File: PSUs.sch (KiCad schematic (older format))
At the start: 26 parts, among them U1 LM2674N-ADJ, U11 MCP4151-103E/P, U12 MCP4151-103E/P, U3 LM2674N-ADJ, U8 MCP6042

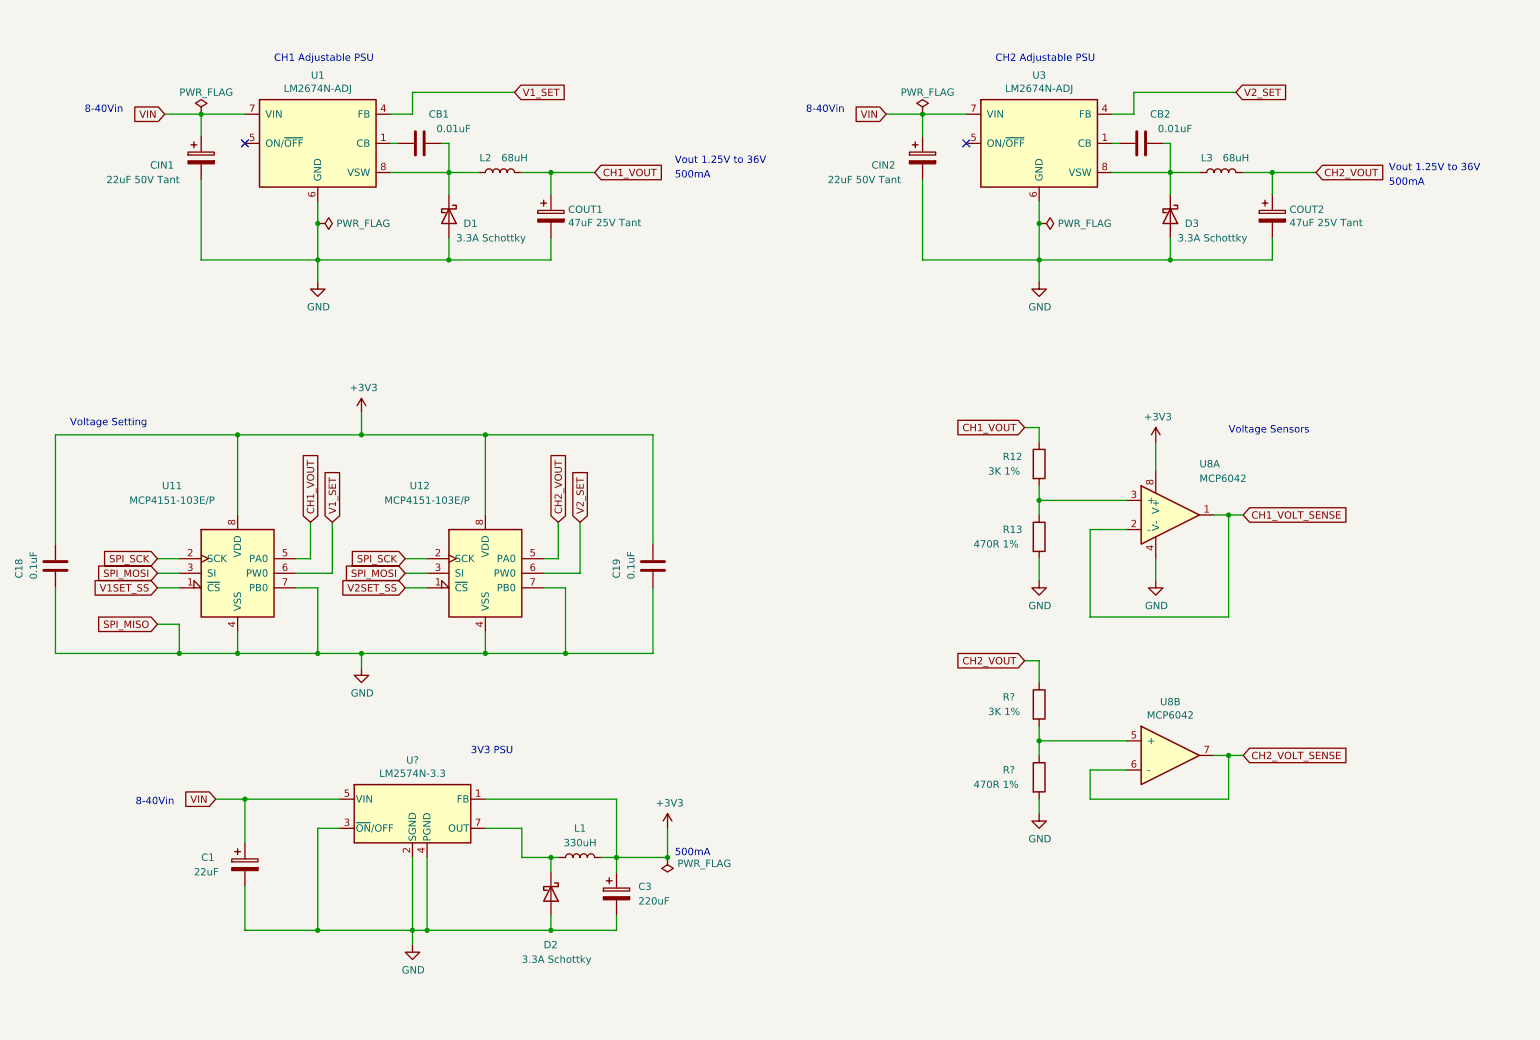
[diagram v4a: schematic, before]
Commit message: fixed some DRC errors
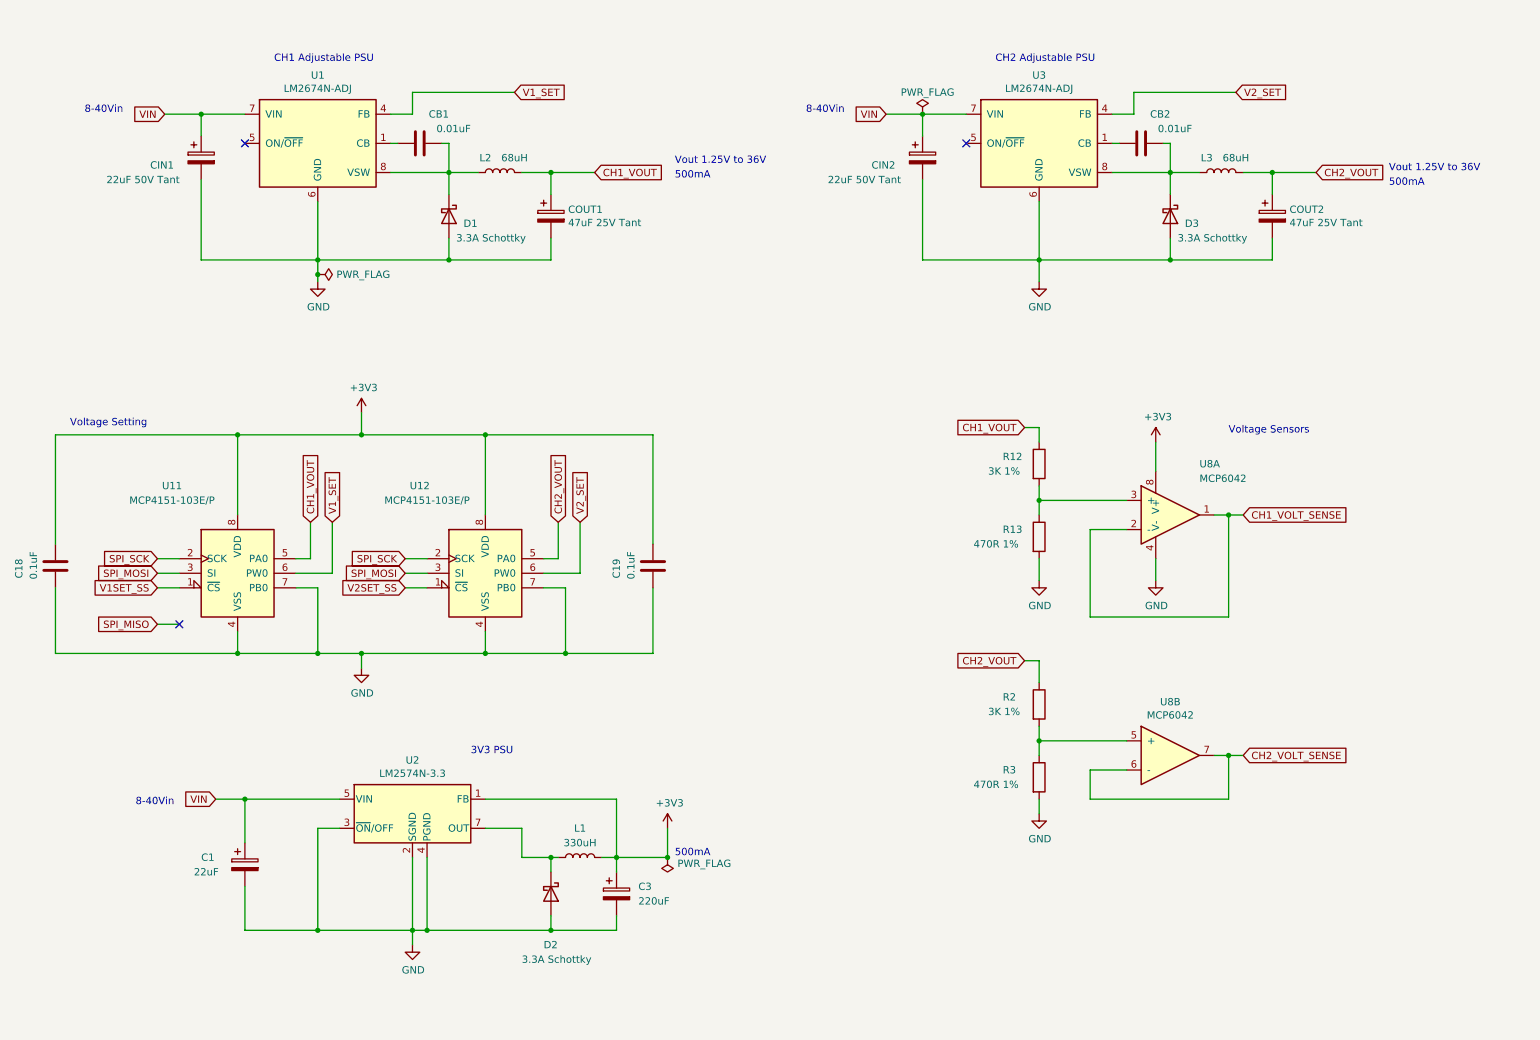
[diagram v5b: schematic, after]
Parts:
- gave numbers to parts that had none: 3
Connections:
- no-connect marks 2 -> 3
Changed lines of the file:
@@
 Wire Wire Line
 	8700 2400 7800 2400
-Wire Wire Line
-	7800 2400 7800 2150
 Connection ~ 8700 2400
 NoConn ~ 7300 1600
@@
 Text Notes 6200 1400 0    50   ~ 0
 8-40Vin
-$Comp
-L power:PWR_FLAG #GNDFLAG?
-U 1 1 605245E4
-P 7800 2150
-AR Path="/605245E4" Ref="#GNDFLAG?"  Part="1"
-AR Path="/604D3BA3/605245E4" Ref="#GNDFLAG0101"  Part="1"
-F 0 "#GNDFLAG0101" H 7800 2225 50  0001 C CNN
-F 1 "PWR_FLAG" V 7800 2278 50  0000 L CNN
-F 2 "" H 7800 2150 50  0001 C CNN
-F 3 "~" H 7800 2150 50  0001 C CNN
-	1    7800 2150
-	0    1    1    0
-$EndComp
-Connection ~ 7800 2150
-Wire Wire Line
-	7800 2150 7800 2000
 Text Notes 7500 1050 0    50   ~ 0
 CH2 Adjustable PSU
 Text Notes 2550 1050 0    50   ~ 0
 CH1 Adjustable PSU
-Wire Wire Line
-	2850 2150 2850 2000
-Connection ~ 2850 2150
-$Comp
-L power:PWR_FLAG #GNDFLAG?
-U 1 1 605245F3
-P 2850 2150
-AR Path="/605245F3" Ref="#GNDFLAG?"  Part="1"
-AR Path="/604D3BA3/605245F3" Ref="#GNDFLAG0102"  Part="1"
-F 0 "#GNDFLAG0102" H 2850 2225 50  0001 C CNN
-F 1 "PWR_FLAG" V 2850 2278 50  0000 L CNN
-F 2 "" H 2850 2150 50  0001 C CNN
-F 3 "~" H 2850 2150 50  0001 C CNN
-	1    2850 2150
-	0    1    1    0
-$EndComp
 Text Notes 1250 1400 0    50   ~ 0
 8-40Vin
-$Comp
-L power:PWR_FLAG #8-40Vin?
-U 1 1 605245FA
-P 2050 1400
-AR Path="/605245FA" Ref="#8-40Vin?"  Part="1"
-AR Path="/604D3BA3/605245FA" Ref="#8-40Vin0102"  Part="1"
-F 0 "#8-40Vin0102" H 2050 1475 50  0001 C CNN
-F 1 "PWR_FLAG" H 1900 1550 50  0000 L CNN
-F 2 "" H 2050 1400 50  0001 C CNN
-F 3 "~" H 2050 1400 50  0001 C CNN
-	1    2050 1400
-	1    0    0    -1
-$EndComp
 $Comp
 L Regulator_Switching:LM2674N-ADJ U?
@@
 Wire Wire Line
 	3350 1600 3400 1600
-Connection ~ 2050 1400
-Wire Wire Line
-	2050 1400 1800 1400
 Wire Wire Line
 	2050 2400 2850 2400
 Wire Wire Line
 	2050 1850 2050 2400
-Wire Wire Line
-	2050 1400 2050 1550
-Wire Wire Line
-	2350 1400 2050 1400
 Wire Wire Line
 	4450 1800 4750 1800
@@
 $EndComp
 Wire Wire Line
-	2850 2400 2850 2550
+	2850 2400 2850 2500
 Text GLabel 1800 1400 0    50   Input ~ 0
 VIN
@@
 NoConn ~ 2350 1600
 Connection ~ 3750 2400
-Wire Wire Line
-	2850 2400 2850 2150
 Wire Wire Line
 	3750 2400 2850 2400
@@
 Wire Wire Line
 	1050 4650 1050 5100
-Wire Wire Line
-	1050 5100 1900 5100
 Connection ~ 2300 5100
 $Comp
@@
 Wire Wire Line
 	4000 3600 3150 3600
-Text GLabel 1750 4900 0    50   Input ~ 0
-SPI_MISO
-Wire Wire Line
-	1750 4900 1900 4900
-Wire Wire Line
-	1900 4900 1900 5100
-Connection ~ 1900 5100
-Wire Wire Line
-	1900 5100 2300 5100
 Text GLabel 1750 4450 0    50   Input ~ 0
 SPI_SCK
@@
 SPI_MOSI
 $Comp
-L power:+3V3 #PWR?
+L power:+3V3 #PWR0103
 U 1 1 600D52AF
 P 5250 6300
-F 0 "#PWR?" H 5250 6150 50  0001 C CNN
+F 0 "#PWR0103" H 5250 6150 50  0001 C CNN
 F 1 "+3V3" H 5265 6473 50  0000 C CNN
 F 2 "" H 5250 6300 50  0001 C CNN
@@
 $EndComp
 $Comp
-L power:+3V3 #PWR?
+L power:+3V3 #PWR0105
 U 1 1 600D6FEA
 P 8600 3650
-F 0 "#PWR?" H 8600 3500 50  0001 C CNN
+F 0 "#PWR0105" H 8600 3500 50  0001 C CNN
 F 1 "+3V3" H 8615 3823 50  0000 C CNN
 F 2 "" H 8600 3650 50  0001 C CNN
@@
 $EndComp
 $Comp
-L power:+3V3 #PWR?
+L power:+3V3 #PWR0107
 U 1 1 600D7AC4
 P 3150 3450
-F 0 "#PWR?" H 3150 3300 50  0001 C CNN
+F 0 "#PWR0107" H 3150 3300 50  0001 C CNN
 F 1 "+3V3" H 3165 3623 50  0000 C CNN
 F 2 "" H 3150 3450 50  0001 C CNN
@@
 $EndComp
 $Comp
-L Device:R R?
+L Device:R R2
 U 1 1 600E45EF
 P 7800 5450
-F 0 "R?" H 7550 5500 50  0000 L CNN
+F 0 "R2" H 7550 5500 50  0000 L CNN
 F 1 "3K 1%" H 7450 5400 50  0000 L CNN
 F 2 "" V 7730 5450 50  0001 C CNN
@@
 $EndComp
 $Comp
-L Device:R R?
+L Device:R R3
 U 1 1 600E4D4D
 P 7800 5950
-F 0 "R?" H 7550 6000 50  0000 L CNN
+F 0 "R3" H 7550 6000 50  0000 L CNN
 F 1 "470R 1%" H 7350 5900 50  0000 L CNN
 F 2 "" V 7730 5950 50  0001 C CNN
@@
 $EndComp
 $Comp
-L Regulator_Switching:LM2574N-3.3 U?
+L Regulator_Switching:LM2574N-3.3 U2
 U 1 1 600E5721
 P 3500 6200
-F 0 "U?" H 3500 6567 50  0000 C CNN
+F 0 "U2" H 3500 6567 50  0000 C CNN
 F 1 "LM2574N-3.3" H 3500 6476 50  0000 C CNN
 F 2 "Package_DIP:DIP-8_W7.62mm" H 3100 6550 50  0001 L CIN
@@
 Wire Wire Line
 	3600 7000 4450 7000
+Wire Wire Line
+	7800 2000 7800 2400
+Wire Wire Line
+	2850 2000 2850 2400
+Wire Wire Line
+	2350 1400 2050 1400
+Wire Wire Line
+	2050 1550 2050 1400
+Connection ~ 2050 1400
+Wire Wire Line
+	2050 1400 1800 1400
+$Comp
+L power:PWR_FLAG #FLG0101
+U 1 1 5FF5E115
+P 2850 2500
+F 0 "#FLG0101" H 2850 2575 50  0001 C CNN
+F 1 "PWR_FLAG" V 2850 2628 50  0000 L CNN
+F 2 "" H 2850 2500 50  0001 C CNN
+F 3 "~" H 2850 2500 50  0001 C CNN
+	1    2850 2500
+	0    1    1    0
+$EndComp
+Connection ~ 2850 2500
+Wire Wire Line
+	2850 2500 2850 2550
+Wire Wire Line
+	1750 4900 1900 4900
+Text GLabel 1750 4900 0    50   Input ~ 0
+SPI_MISO
+Wire Wire Line
+	1050 5100 2300 5100
+NoConn ~ 1900 4900
 $EndSCHEMATC

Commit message: ported over LCD display code, modified schematic as we no longer need some of the I2C expanders
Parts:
- U1, U2, U3: footprint Package_DIP:DIP-8_W7.62mm -> (none)
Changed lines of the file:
@@
 F 0 "U3" H 7800 2067 50  0000 C CNN
 F 1 "LM2674N-ADJ" H 7800 1976 50  0000 C CNN
-F 2 "Package_DIP:DIP-8_W7.62mm" H 7850 1250 50  0001 L CIN
+F 2 "" H 7850 1250 50  0001 L CIN
 F 3 "http://www.ti.com/lit/ds/symlink/lm2674.pdf" H 7800 1600 50  0001 C CNN
 	1    7800 1600
@@
 F 0 "U1" H 2850 2067 50  0000 C CNN
 F 1 "LM2674N-ADJ" H 2850 1976 50  0000 C CNN
-F 2 "Package_DIP:DIP-8_W7.62mm" H 2900 1250 50  0001 L CIN
+F 2 "" H 2900 1250 50  0001 L CIN
 F 3 "http://www.ti.com/lit/ds/symlink/lm2674.pdf" H 2850 1600 50  0001 C CNN
 	1    2850 1600
@@
 F 0 "U2" H 3500 6567 50  0000 C CNN
 F 1 "LM2574N-3.3" H 3500 6476 50  0000 C CNN
-F 2 "Package_DIP:DIP-8_W7.62mm" H 3100 6550 50  0001 L CIN
+F 2 "" H 3100 6550 50  0001 L CIN
 F 3 "http://www.national.com/ds/LM/LM2574.pdf" H 3500 6200 50  0001 C CNN
 	1    3500 6200

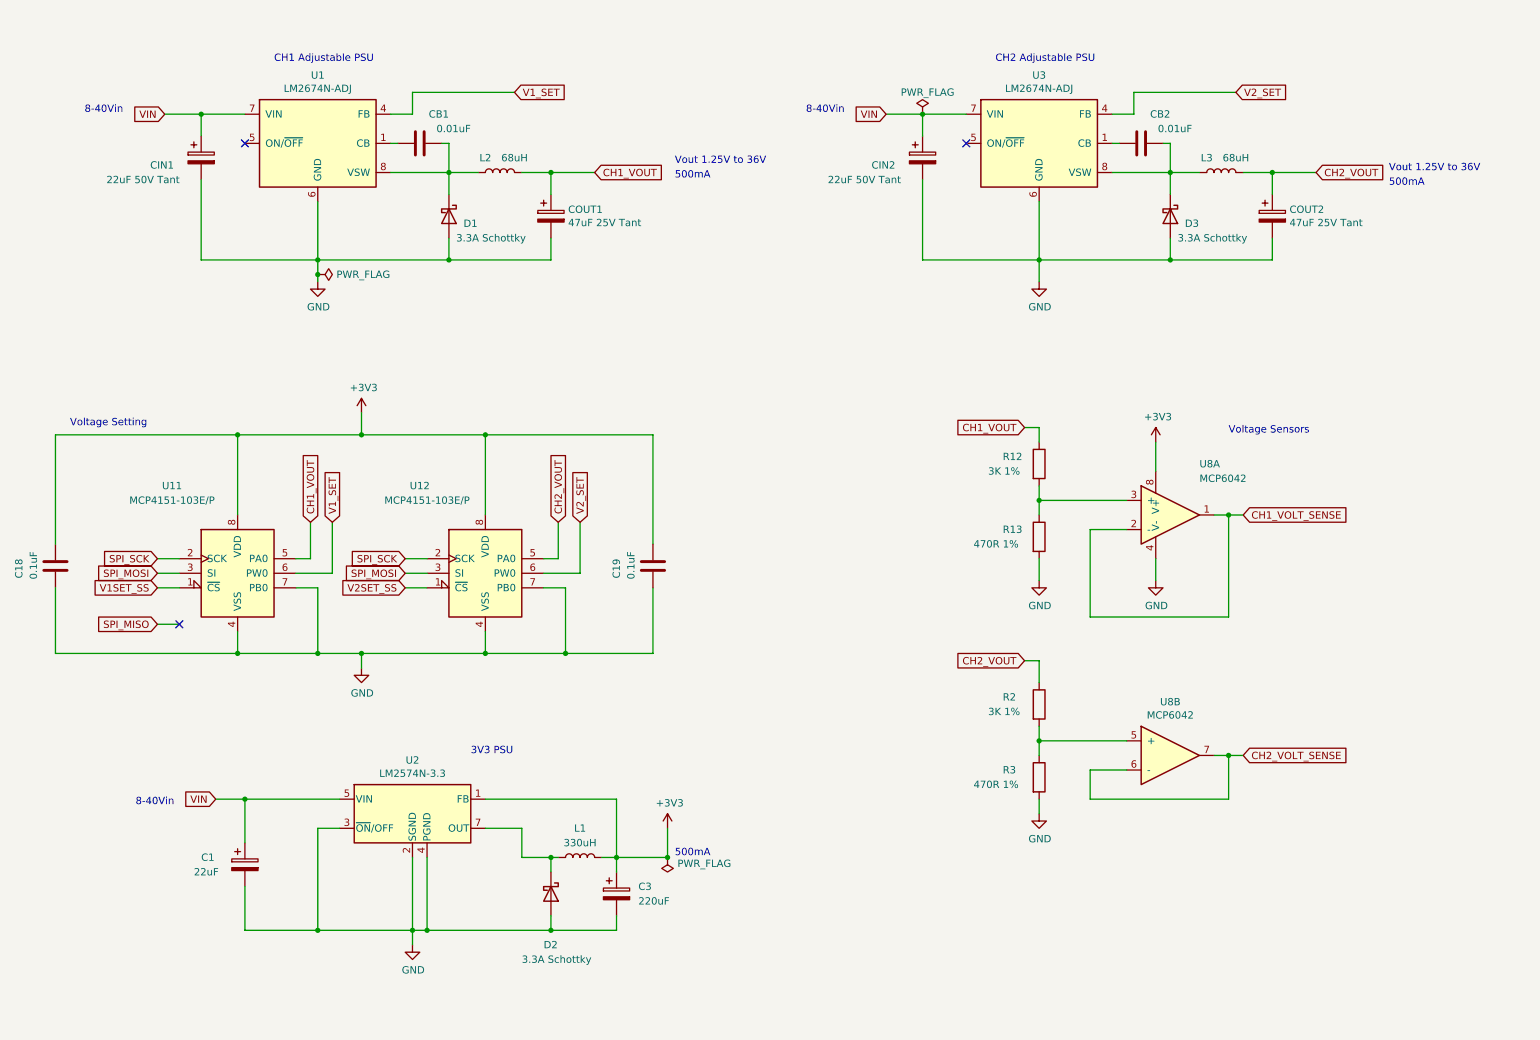
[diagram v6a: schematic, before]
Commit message: modifications to voltage reading schematic, mocked up code
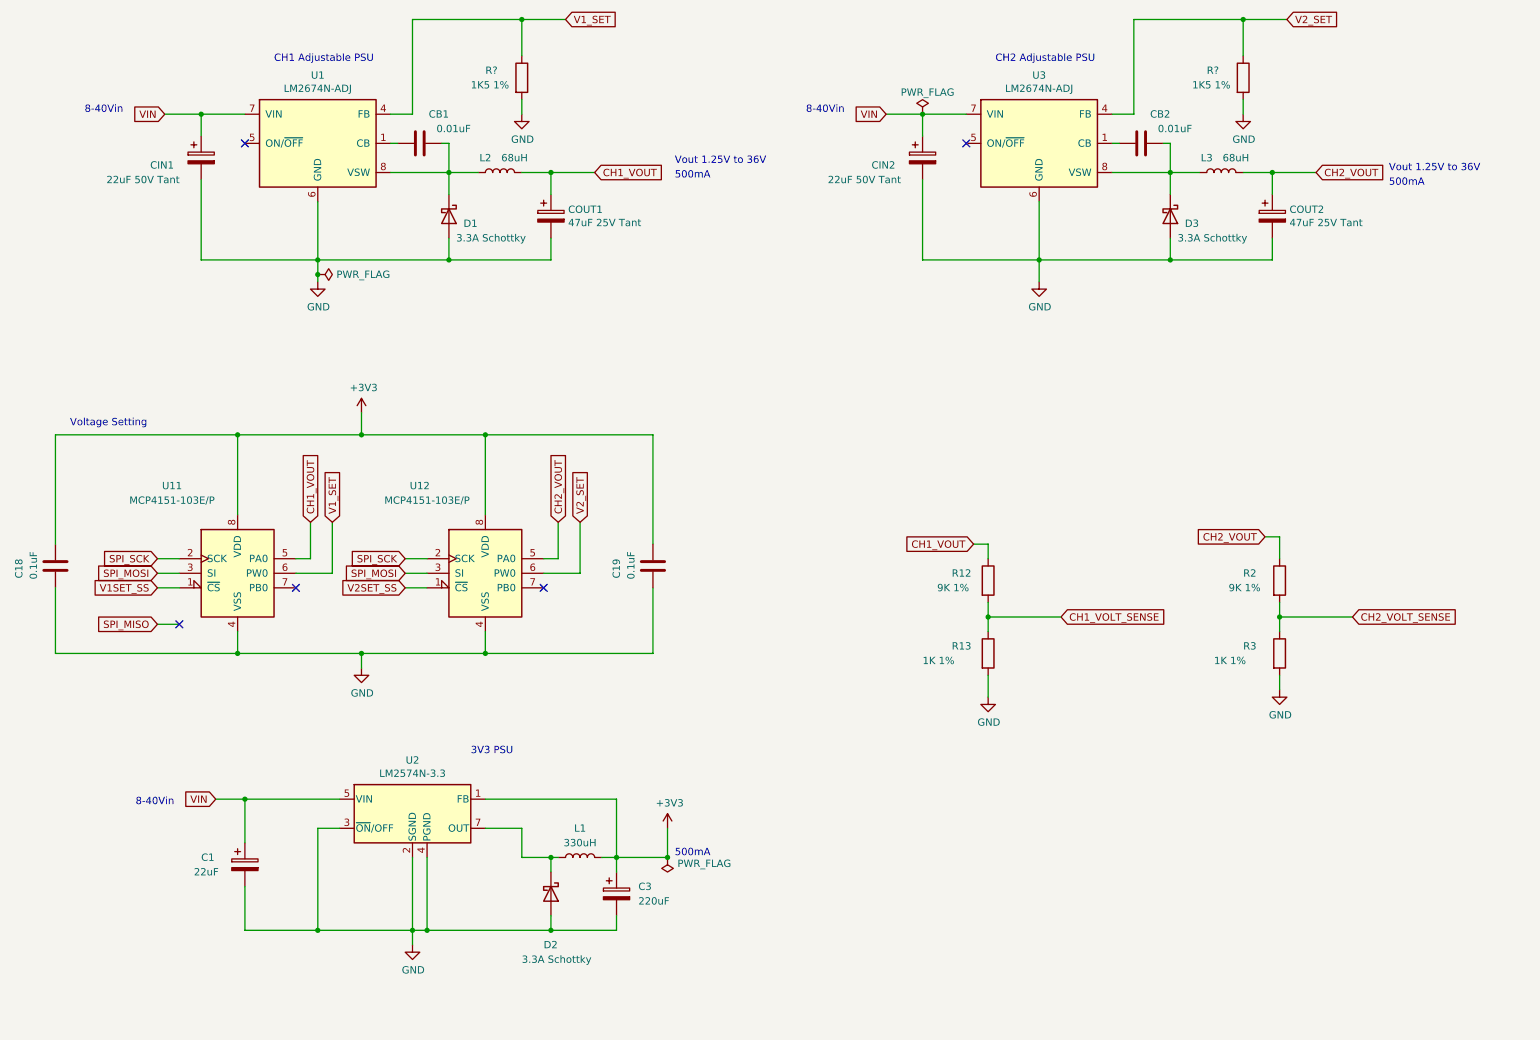
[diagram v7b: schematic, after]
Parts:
- removed U8: MCP6042, Package_TO_SOT_SMD:SOT-23-8_Handsoldering, symbol OpAmps:MCP6042
- added R? (x2): 1K5 1%, symbol Device:R
- R12, R2: value 3K 1% -> 9K 1%
- R13, R3: value 470R 1% -> 1K 1%
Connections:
- net CH1_VOLT_SENSE: now also R12.2, R13.1
- net CH2_VOLT_SENSE: now also R2.2, R3.1
- net GND: now also R?.2, R?.2; no longer U11.7 (PB0), U12.7 (PB0)
- net V1_SET: now also R?.1
- net V2_SET: now also R?.1
- no-connect marks 3 -> 5
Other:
- note removed: "Voltage Sensors"
- moved on the sheet: R12, R13, R2, R3
